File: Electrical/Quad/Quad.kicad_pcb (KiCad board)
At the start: 2 copper layers, 140 x 70 mm, 133 parts, among them J101 01x04, J102 01x04, J103 01x03, J104 01x03, J201 01x03, J202 01x04, J203 01x03, J204 01x04, J205 01x03, J206 USB_OTG, J207 01x04, J208 01x02, J209 01x04, J210 01x02, J211 01x02, J212 4PostTerm, J213 2PostTerm, J214 2PostTerm, J215 2PostTerm, J216 2PostTerm, J217 2PostTerm, J218 01x02, J219 01x02, Q201 FDC6420C, Q202 FDG1024NZ, Q301 FDC6420C, Q401 FDC6420C, Q501 FDC6420C, Q601 FDC6420C, U201 TPD4S012, U202 ACS712ELCTR-05B-T, U203 ACS712ELCTR-05B-T, U204 24LC256, U205 LM2576HVS-ADJ, U206 LM2576HVS-ADJ

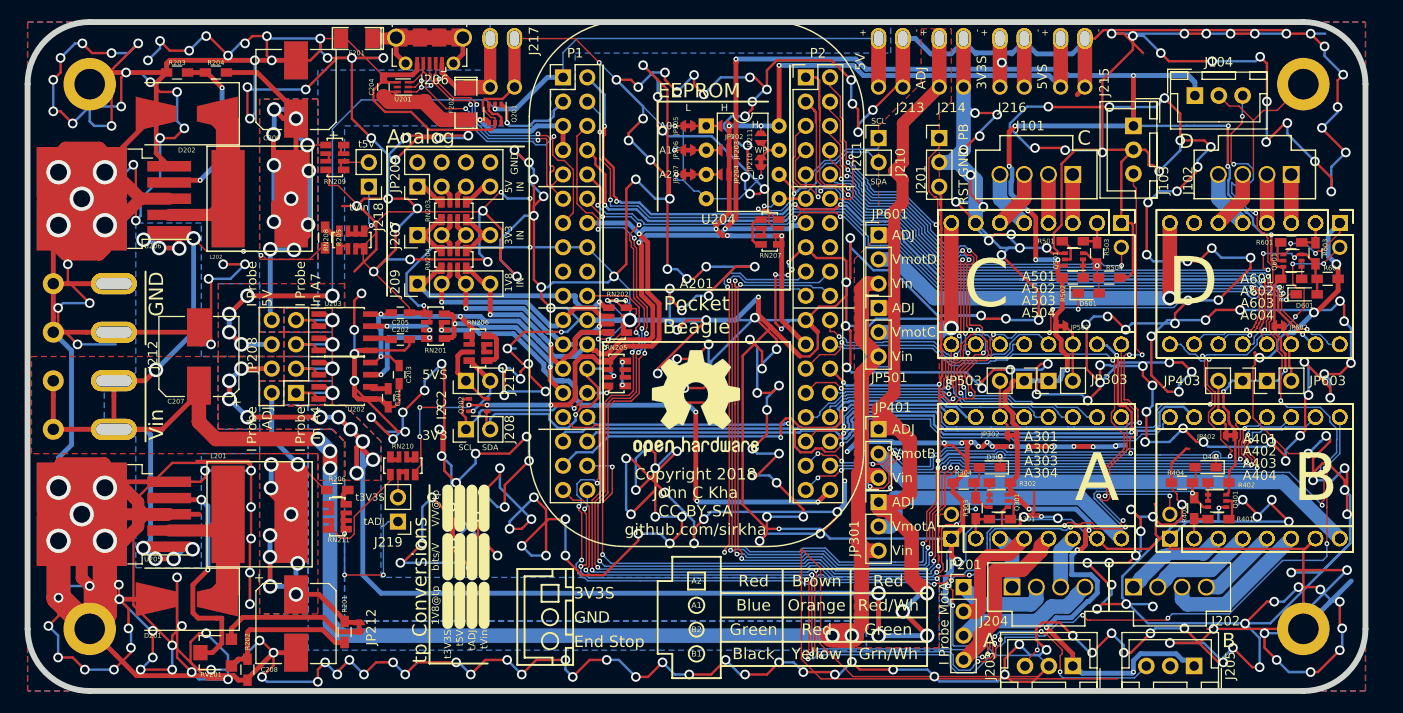
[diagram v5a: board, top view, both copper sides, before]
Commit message: Used bigger capacitor footprints to allow for 1000 uF electrolytics at 50V
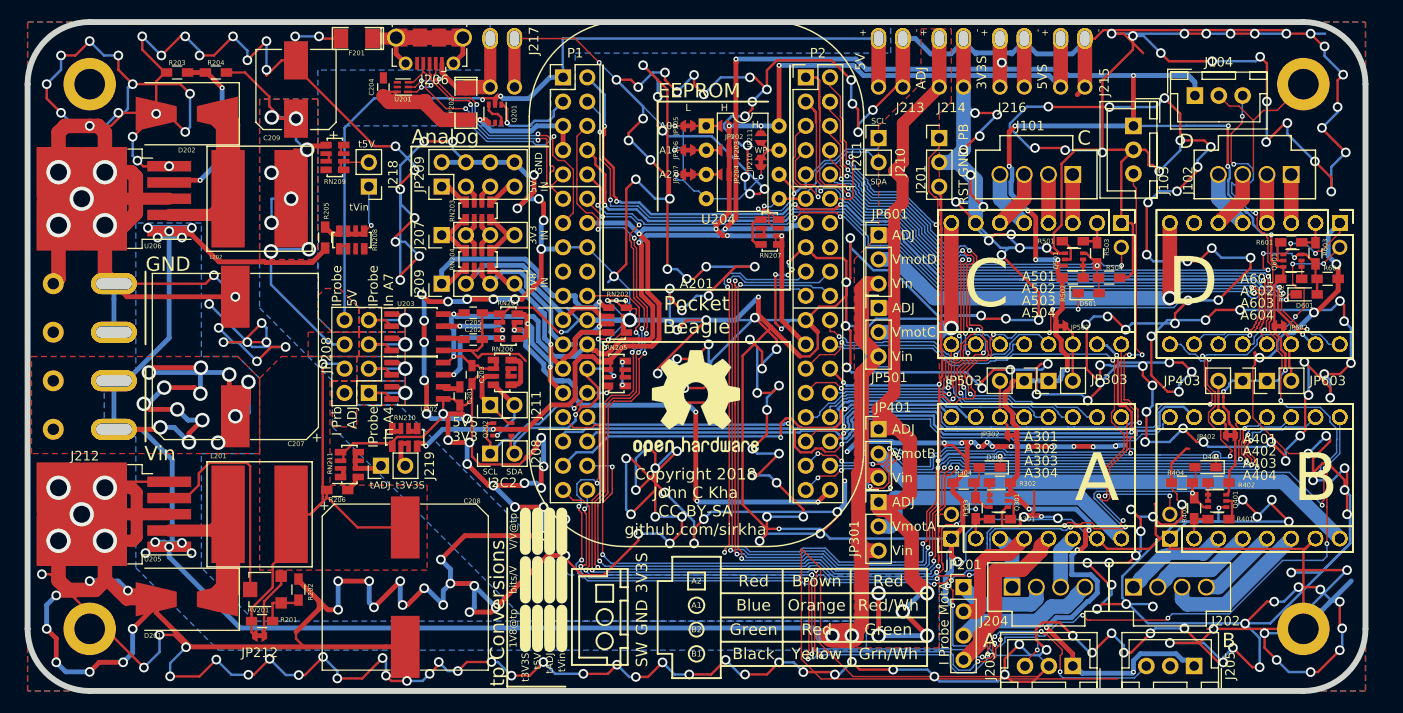
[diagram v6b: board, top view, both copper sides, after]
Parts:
- C207, C208: footprint Capacitors_SMD:CP_Elec_8x10 -> footprints:CP_Elec_17x17
- moved C208 12.0 mm to (69.5, 124.1)
- moved JP212 10.5 mm to (54.3, 129.2), turned to 180 degrees
- moved R202 9.94 mm to (58.3, 124.4), turned to 270 degrees
- moved R201 8.71 mm to (54.5, 127.7), turned to 0 degrees
- moved RV201 8.41 mm to (54.9, 124.4)
- moved C202 7.62 mm to (76.6, 98.2)
- moved C205 7.62 mm to (76.6, 95.4)
- moved RN201 7.62 mm to (80.3, 96.8)
- moved U202 7.62 mm to (70.8, 102.5)
- moved U203 7.62 mm to (70.8, 97.5)
- moved C203 7.62 mm to (76.5, 101.9)
- moved JP208 7.62 mm to (65.7, 103.8)
- moved C201 7.50 mm to (75.2, 104.1)
- moved J219 6.11 mm to (67.0, 111.4), turned to 90 degrees
- moved RN211 5.61 mm to (63.7, 111.3), turned to 90 degrees
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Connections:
- JP208 pad b1: /Common/IP_vadj -> Vadj
- JP208 pad b2: Vadj -> /Common/IP_vadj
- JP208 pad b3: +5V -> /Common/IP_5V
- JP208 pad b4: /Common/IP_5V -> +5V
- RN211 pad 1: Net-(RN211-Pad1) -> Net-(R206-Pad1)
- RN211 pad 2: Net-(RN211-Pad1) -> Net-(J219-Pad1)
- RN211 pad 3: GND -> Net-(J219-Pad1)
- RN211 pad 4: GND -> Net-(J219-Pad1)
- RN211 pad 5: Net-(J219-Pad1) -> GND
- RN211 pad 6: Net-(J219-Pad1) -> GND
- RN211 pad 7: Net-(J219-Pad1) -> Net-(RN211-Pad7)
- RN211 pad 8: Net-(R206-Pad1) -> Net-(RN211-Pad7)
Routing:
- net GND: track 2865.7 -> 2508.6 mm, vias 427 -> 393
- net Vadj: track 204.5 -> 98.5 mm, vias 15 -> 5
- net Vin: track 239.8 -> 273.4 mm, vias 16 -> 25
- net +5V: track 104.8 -> 89.0 mm, vias 6 -> 2
- net Net-(J219-Pad1): track 18.2 -> 4.39 mm, vias 3 -> 0
- net Net-(R201-Pad2): track 15.6 -> 4.71 mm
- net /Common/IP_5V: track 66.4 -> 57.0 mm, vias 11 -> 8
- net Net-(JP212-Pad1): track 15.6 -> 6.97 mm
- net /Common/ain7: track 56.7 -> 49.9 mm
- net /Common/ain4: track 20.3 -> 13.6 mm
- net 5VS: track 133.3 -> 126.8 mm, vias 6 -> 5
- net 3V3S: track 357.9 -> 353.1 mm, vias 31 -> 27
- net /Common/i2c2_sda: track 25.4 -> 22.4 mm
- net /Common/ain3: track 25.4 -> 22.4 mm, vias 2 -> 1
- net /Common/ain1: track 24.2 -> 22.5 mm, vias 1 -> 0
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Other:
- board text added: "I Prb ADJ"
- board text added: "IProbe 5V"
- board text added: "IProbe In A4"
- board text added: "IProbe In A7"
- board text added: "SW"
- board text removed: "End Stop"
- board text removed: "I Probe 5V"
- board text removed: "I Probe ADJ"
- board text removed: "I Probe In A4"
- board text removed: "I Probe In A7"

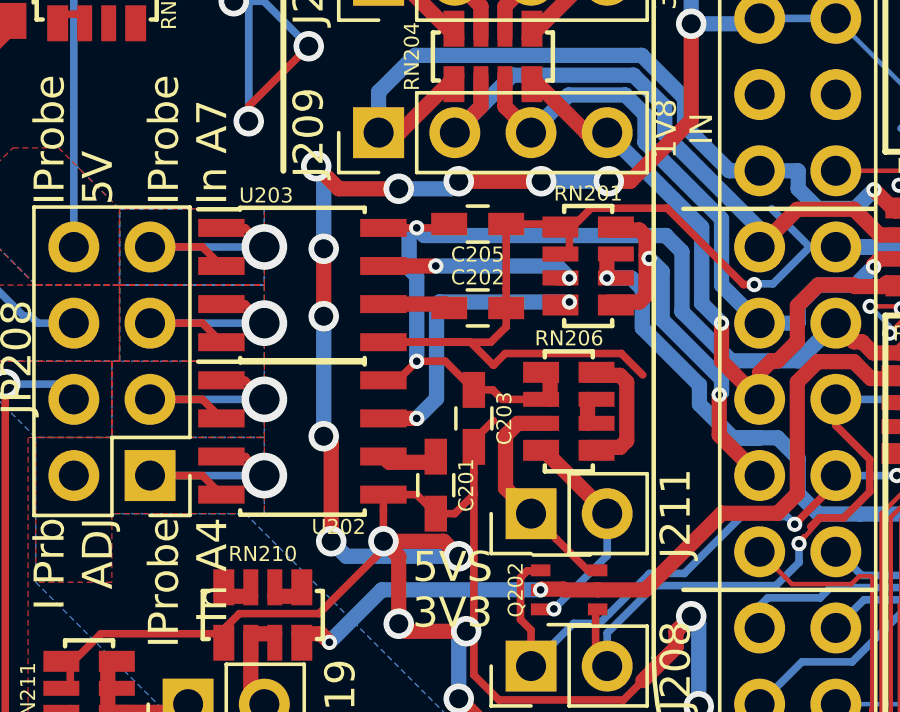
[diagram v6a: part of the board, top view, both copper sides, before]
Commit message: ACS712 -> ACS723
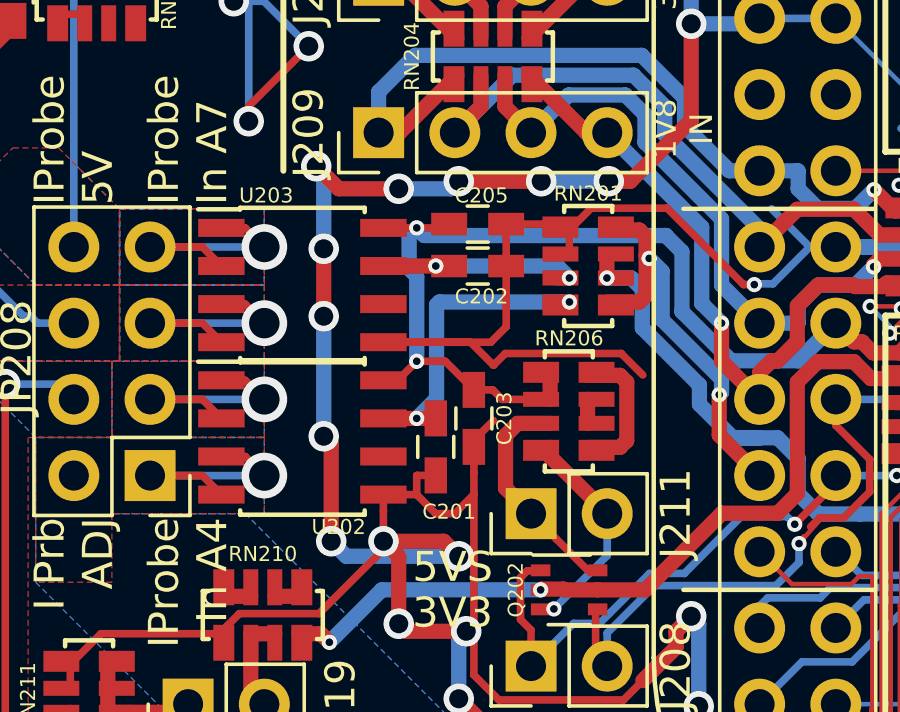
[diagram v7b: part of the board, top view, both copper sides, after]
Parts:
- U202, U203: value ACS712ELCTR-05B-T -> ACS723LLCTR-05AB-T
- moved C202 1.40 mm to (76.6, 96.8)
- moved C201 1.27 mm to (75.2, 102.9)
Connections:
- RN201 pad 7: Net-(RN201-Pad7) -> Net-(C202-Pad1)
- RN201 pad 8: Net-(RN201-Pad8) -> Net-(C201-Pad1)
- U202 pad 6: Net-(C201-Pad1) -> (no net)
- U202 pad 7: Net-(RN201-Pad8) -> Net-(C201-Pad1)
- U203 pad 6: Net-(C202-Pad1) -> (no net)
- U203 pad 7: Net-(RN201-Pad7) -> Net-(C202-Pad1)
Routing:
- net Net-(RN201-Pad8): track 9.64 -> 0.00 mm, vias 2 -> 0
- net Net-(C201-Pad1): track 1.95 -> 10.3 mm, vias 0 -> 2
- net Net-(RN201-Pad7): track 6.81 -> 0.00 mm, vias 2 -> 0
- net Net-(C202-Pad1): track 2.24 -> 7.26 mm, vias 0 -> 2
- net GND: track 2508.6 -> 2509.9 mm

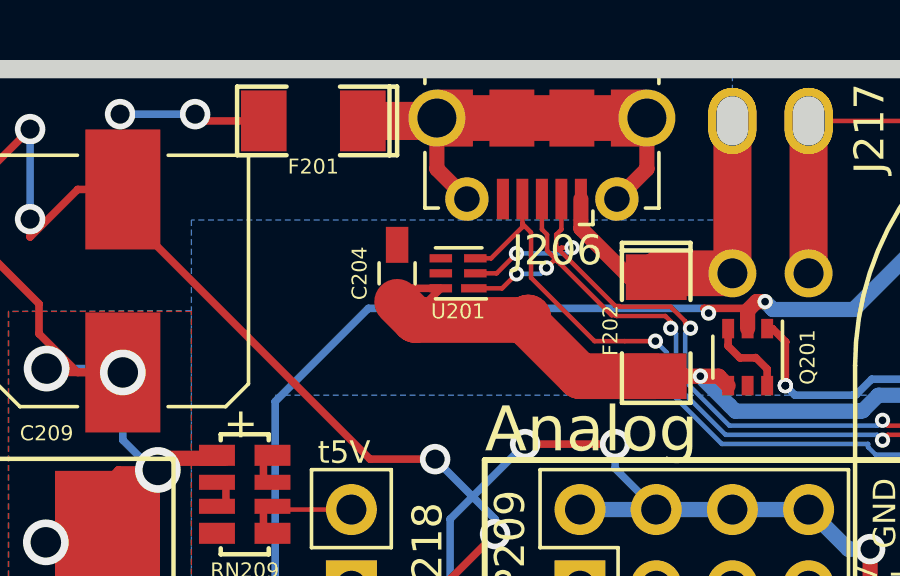
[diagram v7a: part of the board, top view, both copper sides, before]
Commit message: FB <> Fuse; FB == Ferrite Bead
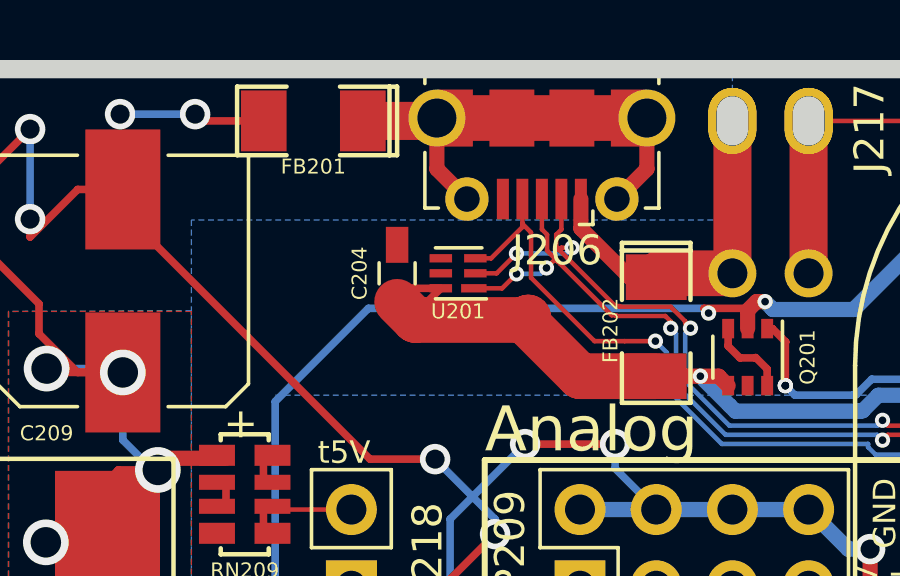
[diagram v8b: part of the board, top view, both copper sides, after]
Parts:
- FB201: renamed from F201; value Fuse -> 120
- FB202: renamed from F202; value Fuse -> 120
